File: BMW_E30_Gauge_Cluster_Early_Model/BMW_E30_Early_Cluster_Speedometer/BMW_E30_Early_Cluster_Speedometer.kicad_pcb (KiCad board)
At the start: 2 copper layers, 15 parts, among them J1 Conn_01x06_Socket, M1 Odometer, U1 UAF2115

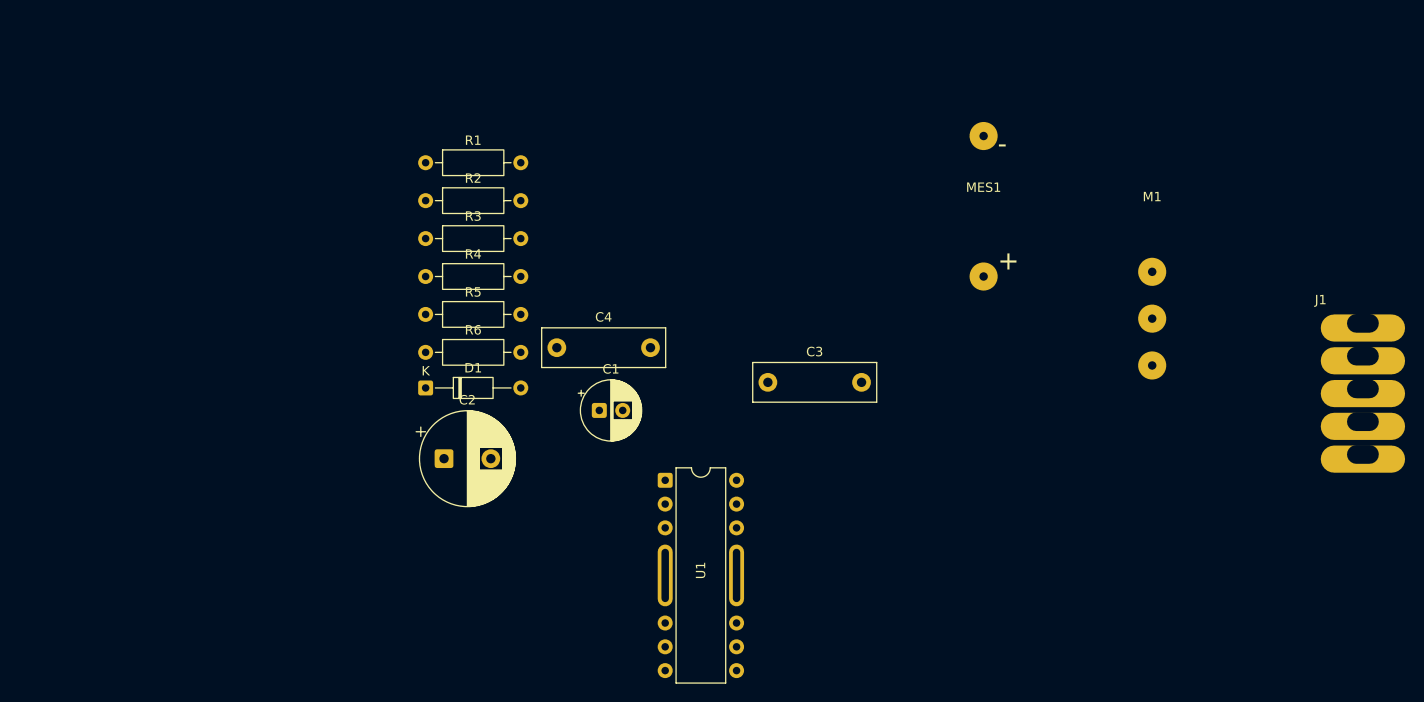
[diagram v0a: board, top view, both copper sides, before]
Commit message: Layout Updates
Drew out board cut outlines and 2 clearance holes for the speedometer mounts. Added footprint for O2 sensor connector as well.
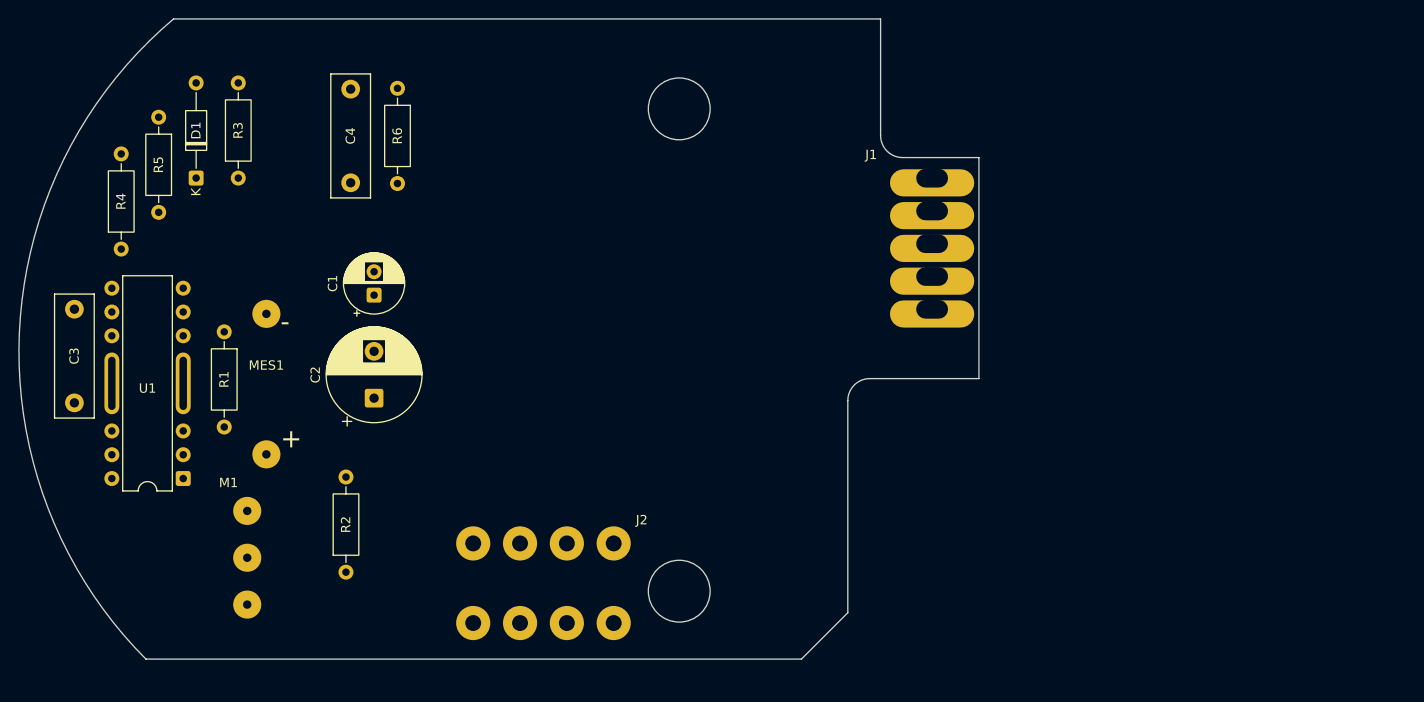
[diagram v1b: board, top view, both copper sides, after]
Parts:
- added J2: Conn_01x04_Socket, BMW_Cluster_Connectors:BMW_1372218, F.Cu at (156.5, 91.0)
- moved M1 99.9 mm to (132.4, 92.5)
- moved MES1 78.9 mm to (134.4, 74.0)
- moved C3 74.5 mm to (113.9, 66.0), turned to -90 degrees
- moved U1 62.2 mm to (121.7, 74.5), turned to 180 degrees
- moved J1 48.5 mm to (205.5, 59.0)
- moved R2 40.6 mm to (142.9, 94.1), turned to 90 degrees
- moved R5 35.4 mm to (122.9, 45.5), turned to -90 degrees
- moved D1 33.2 mm to (126.9, 52.0), turned to 90 degrees
- moved R4 32.6 mm to (118.9, 59.6), turned to 90 degrees
- moved R6 28.3 mm to (148.4, 42.4), turned to -90 degrees
- moved C4 28.2 mm to (143.4, 52.5), turned to 90 degrees
- moved R1 28.1 mm to (129.9, 68.4), turned to -90 degrees
- moved C1 27.0 mm to (145.9, 64.5), turned to 90 degrees
- moved R3 21.0 mm to (131.4, 52.0), turned to 90 degrees
- moved C2 9.88 mm to (145.9, 75.5), turned to 90 degrees
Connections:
- M1 pad 2: Net-(U1-M2) -> +12 T15_ACC
- M1 pad 3: +12 T15_ACC -> Net-(U1-M2)
- R3 pad 2: GND -> Net-(J1-Pin_3)
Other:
- board outline added: 102.5 x 68.3 mm

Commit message: Component Layout
Rough layout of components completed
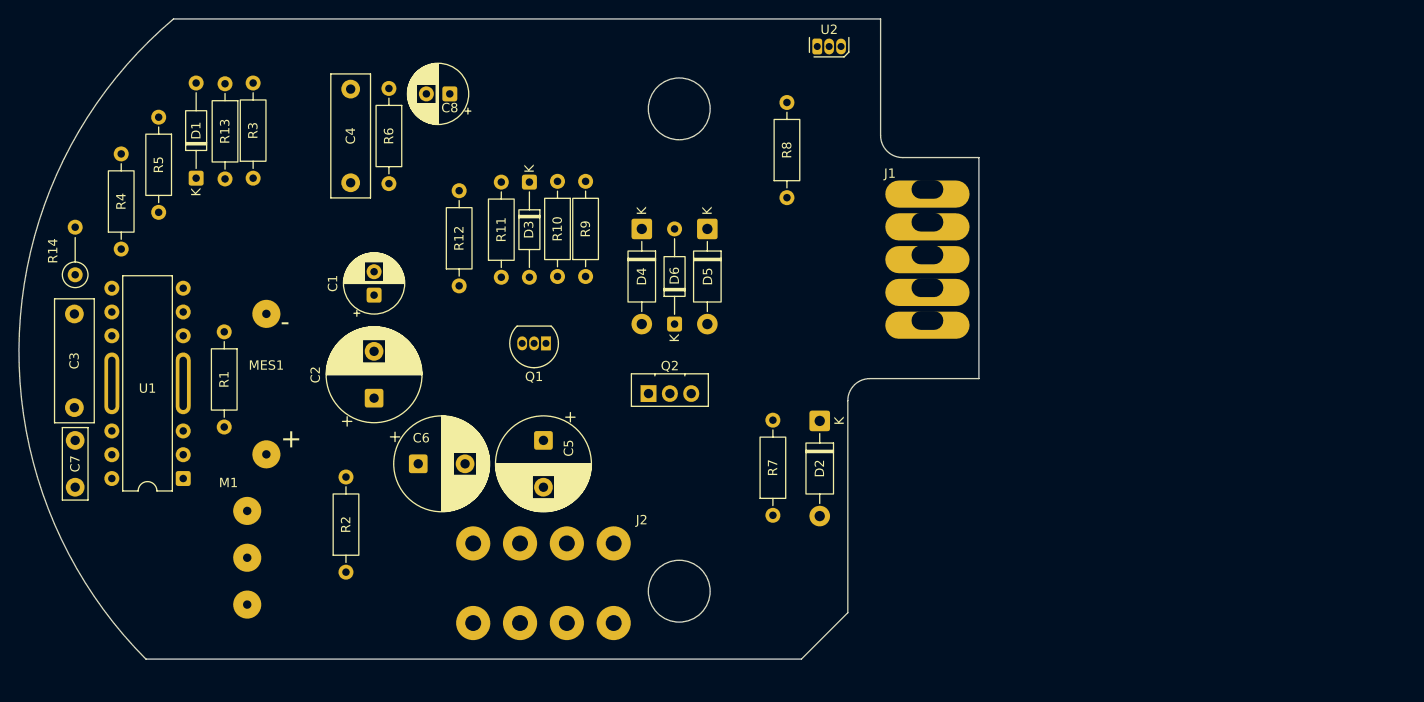
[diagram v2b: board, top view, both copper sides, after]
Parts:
- added C5: 100u, Capacitor_THT:CP_Radial_D10.0mm_P5.00mm, F.Cu at (164.0, 80.0)
- added C6: ?, Capacitor_THT:CP_Radial_D10.0mm_P5.00mm, F.Cu at (150.6, 82.5)
- added C7: 0.47u, Capacitor_THT:C_Disc_D7.5mm_W2.5mm_P5.00mm, F.Cu at (114.0, 80.0)
- added C8: 47u, Capacitor_THT:CP_Radial_D6.3mm_P2.50mm, F.Cu at (154.0, 43.0)
- added D2: 1N4005, Diode_THT:D_DO-41_SOD81_P10.16mm_Horizontal, F.Cu at (193.5, 77.9)
- added D3: 1N4148, Diode_THT:D_DO-35_SOD27_P10.16mm_Horizontal, F.Cu at (162.5, 52.4)
- added D4: 1N4005, Diode_THT:D_DO-41_SOD81_P10.16mm_Horizontal, F.Cu at (174.5, 57.4)
- added D5: 1N4005, Diode_THT:D_DO-41_SOD81_P10.16mm_Horizontal, F.Cu at (181.5, 57.4)
- added D6: D_Zener, Diode_THT:D_DO-35_SOD27_P10.16mm_Horizontal, F.Cu at (178.0, 67.6)
- added Q1: BC327-40, Package_TO_SOT_THT:TO-92_Inline, F.Cu at (164.3, 69.6)
- added Q2: BD135, Package_TO_SOT_THT:TO-126-3_Vertical, F.Cu at (175.2, 75.0)
- added R10: 10R, Resistor_THT:R_Axial_DIN0207_L6.3mm_D2.5mm_P10.16mm_Horizontal, F.Cu at (165.5, 52.3)
- added R11: 330R, Resistor_THT:R_Axial_DIN0207_L6.3mm_D2.5mm_P10.16mm_Horizontal, F.Cu at (159.5, 62.6)
- added R12: 10k, Resistor_THT:R_Axial_DIN0207_L6.3mm_D2.5mm_P10.16mm_Horizontal, F.Cu at (155.0, 63.5)
- added R13: 47k, Resistor_THT:R_Axial_DIN0207_L6.3mm_D2.5mm_P10.16mm_Horizontal, F.Cu at (130.0, 41.9)
- added R14: ?, Resistor_THT:R_Axial_DIN0207_L6.3mm_D2.5mm_P5.08mm_Vertical, F.Cu at (114.0, 62.3)
- added R7: 30R, Resistor_THT:R_Axial_DIN0207_L6.3mm_D2.5mm_P10.16mm_Horizontal, F.Cu at (188.5, 88.0)
- added R8: 510R?, Resistor_THT:R_Axial_DIN0207_L6.3mm_D2.5mm_P10.16mm_Horizontal, F.Cu at (190.0, 54.1)
- added R9: 3k, Resistor_THT:R_Axial_DIN0207_L6.3mm_D2.5mm_P10.16mm_Horizontal, F.Cu at (168.5, 62.5)
- added U2: UGS 3020, Package_TO_SOT_THT:TO-92S, F.Cu at (193.2, 37.9)
- moved J1 5.82 mm to (205.0, 53.2)
- moved R3 1.59 mm to (133.0, 52.0)
- moved R6 0.92 mm to (147.5, 42.4)
- moved C3 0.51 mm to (113.9, 66.5)
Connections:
- J1 pad 12: unconnected-(J1-Pin_1-Pad12) -> D+

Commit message: Schematic & Layout Changes
Made a few changes to the schematic, changing C2 and C8 connections. Locked in the galvanometer and odometer stepper footprint locations on the board.
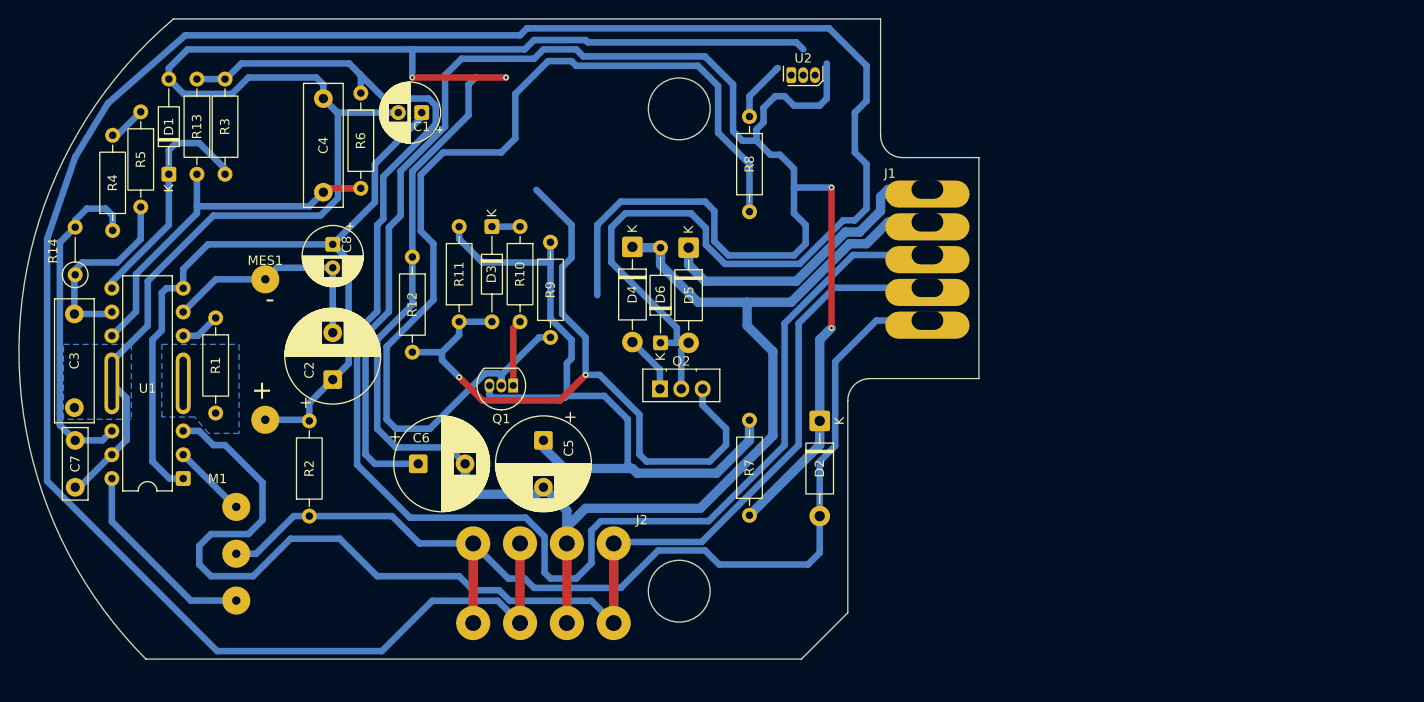
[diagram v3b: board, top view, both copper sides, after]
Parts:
- moved C8 20.4 mm to (141.5, 59.1), turned to -90 degrees
- moved C1 20.1 mm to (151.0, 45.0), turned to 180 degrees
- moved MES1 11.2 mm to (134.3, 62.8)
- moved R9 7.50 mm to (164.8, 69.0)
- moved R2 7.16 mm to (139.0, 88.1)
- moved R11 6.54 mm to (155.0, 67.3)
- moved R10 6.27 mm to (161.5, 57.2)
- moved D3 6.21 mm to (158.5, 57.2)
- moved R12 5.87 mm to (150.0, 60.4), turned to -90 degrees
- moved Q1 5.70 mm to (160.8, 74.1)
- moved C2 4.84 mm to (141.5, 73.5)
- moved R8 4.27 mm to (186.0, 55.6)
- moved U2 4.13 mm to (190.5, 41.0)
- moved C4 3.09 mm to (140.5, 53.5)
- moved R13 3.04 mm to (127.0, 41.4)
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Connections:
- C2 pad 2: GND -> Net-(MES1--)
- C6 pad 1: Net-(Q1-E) -> T15_Protected
- C8 pad 2: GND -> Net-(MES1--)
- R4 pad 1: UAF_8 -> UAF_10
- R5 pad 2: UAF_10 -> UAF_8
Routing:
- net GND: track 0.00 -> 338.5 mm, vias 0 -> 2
- net O2_sensor: track 0.00 -> 270.6 mm
- net T15_Protected: track 0.00 -> 199.0 mm, vias 0 -> 2
- net Net-(J1-Pin_3): track 0.00 -> 164.1 mm
- net Net-(J1-Pin_4): track 0.00 -> 135.7 mm
- net +12 T15_ACC: track 0.00 -> 111.2 mm
- net Net-(Q1-B): track 0.00 -> 108.5 mm
- net Net-(MES1-+): track 0.00 -> 88.1 mm
- net Net-(D3-A): track 0.00 -> 81.6 mm, vias 0 -> 2
- net Net-(Q1-E): track 0.00 -> 79.6 mm
- net UAF_9: track 0.00 -> 39.3 mm
- net UAF_10: track 0.00 -> 35.6 mm
- net D+: track 0.00 -> 33.0 mm
- net UAF_7: track 0.00 -> 25.3 mm
- net Net-(MES1--): track 0.00 -> 24.9 mm
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- added copper zone on B.Cu, net GND

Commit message: Layout Updates
Added and located final mounting holes on the board.
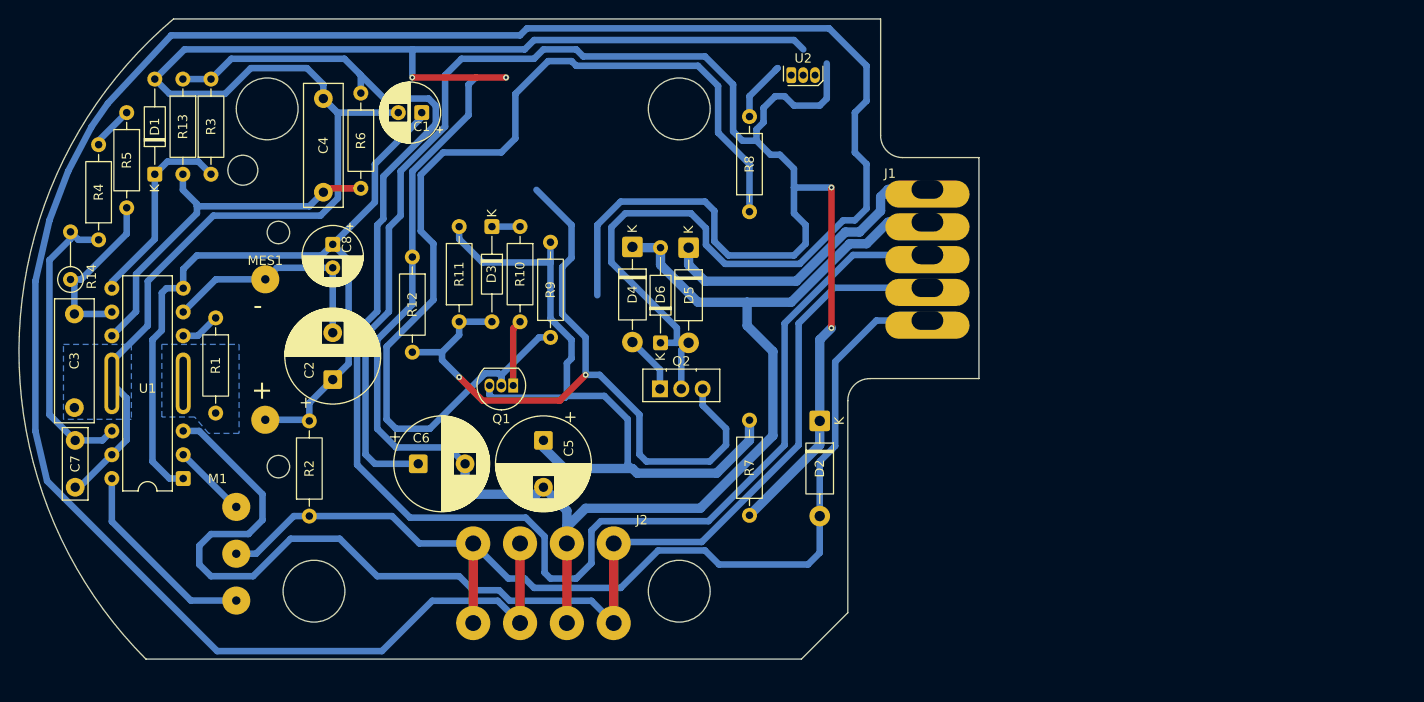
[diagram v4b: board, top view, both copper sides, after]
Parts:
- moved R4 1.80 mm to (116.5, 58.6)
- moved R5 1.50 mm to (119.5, 45.0)
- moved D1 1.50 mm to (122.5, 51.6)
- moved R13 1.50 mm to (125.5, 41.4)
- moved R3 1.50 mm to (128.5, 51.6)
- moved R14 0.71 mm to (113.5, 62.8)
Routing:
- net UAF_7: track 25.3 -> 21.2 mm
- net UAF_10: track 35.6 -> 32.0 mm
- net GND: track 338.5 -> 341.7 mm
- net Net-(J1-Pin_3): track 164.1 -> 166.1 mm
- net UAF_8: track 20.6 -> 18.7 mm
- net O2_sensor: track 270.6 -> 271.4 mm
- net Net-(J1-Pin_4): track 135.7 -> 135.0 mm
- net Net-(R4-Pad2): track 4.04 -> 4.66 mm
- net UAF_9: track 39.3 -> 39.9 mm
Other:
- outline, holes or cut-outs redrawn
